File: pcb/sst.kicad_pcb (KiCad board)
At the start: 2 copper layers, 80 x 85 mm, 36 parts, among them X1 CONN_INPUTS, X2 CONN_PWR, X3 CONN_SPI, X4 CONN_I2C, X5 CONN_INPUTS

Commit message: переместил компонент разъёма для ШИМ
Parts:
- moved X5 0.71 mm to (254.8, 145.8)
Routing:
- net GND: track 384.9 -> 382.1 mm
- net Vbat: track 148.7 -> 145.8 mm
- net /<NO NET>: track 50.9 -> 49.3 mm
- net Net-(DD1-PB1): track 19.8 -> 21.3 mm
- net Net-(DD1-PD7): track 27.0 -> 28.2 mm
- net Net-(DD1-PB3): track 30.3 -> 29.4 mm
- net Net-(VD1-A): track 17.9 -> 18.6 mm
- net Net-(DD1-PD5): track 27.2 -> 26.7 mm

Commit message: moved board and set grid origin
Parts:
- moved R6 102.2 mm to (196.5, 137.2)
- moved R8 102.2 mm to (196.5, 105.2)
- moved C1 101.9 mm to (146.9, 100.7)
- moved C2 101.9 mm to (158.3, 112.7)
- moved C3 101.9 mm to (174.8, 98.7)
- moved C4 101.9 mm to (154.3, 151.7)
- moved C5 101.9 mm to (152.0, 141.2)
- moved DA1 101.9 mm to (142.7, 114.6)
- moved HA1 101.9 mm to (139.8, 149.5)
- moved R1 101.9 mm to (180.6, 109.7)
- moved R10 101.9 mm to (131.8, 133.4)
- moved R11 101.9 mm to (133.2, 157.2)
- moved R12 101.9 mm to (143.8, 131.2)
- moved R14 101.9 mm to (137.8, 131.1)
- moved R3 101.9 mm to (179.8, 129.0)
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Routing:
- net Net-(DD1-PC0): track 31.0 -> 29.8 mm
- net Net-(DD1-PB3): track 29.4 -> 30.0 mm

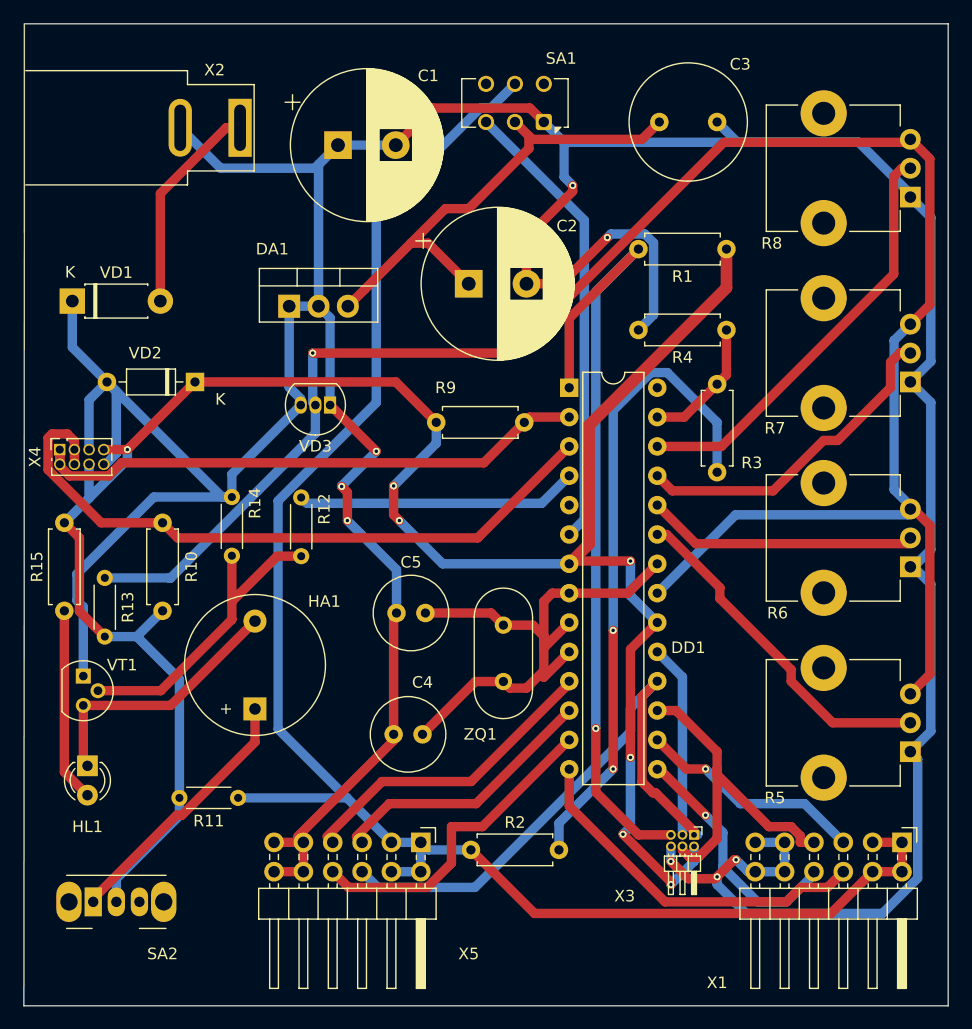
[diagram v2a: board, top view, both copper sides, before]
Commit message: changed geometry, so the demensions would be 80
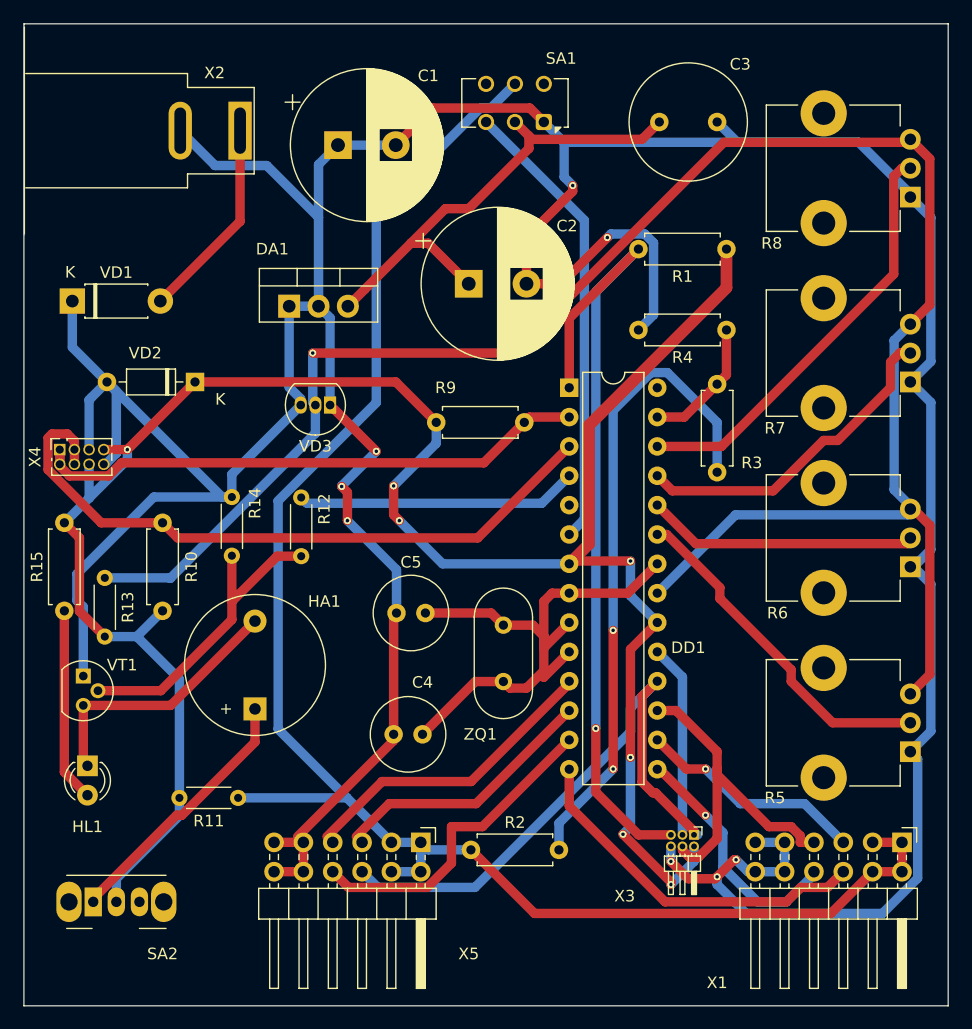
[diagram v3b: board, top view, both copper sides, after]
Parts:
- moved X2 0.25 mm to (138.5, 99.4)
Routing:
- net Net-(VD1-A): track 18.6 -> 17.6 mm
- net GND: track 382.1 -> 381.2 mm
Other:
- outline, holes or cut-outs redrawn
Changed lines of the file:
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@@
 	)
 	(footprint "Connector_BarrelJack:BarrelJack_SwitchcraftConxall_RAPC10U_Horizontal"
-		(locked yes)
 		(layer "F.Cu")
-		(at 138.4656 99.1644)
+		(at 138.4656 99.4144)
 		(descr "DC Power Jack, 13A, 24V, Panel Mount,Through-hole, https://www.switchcraft.com/Drawings/RAPC10U_CD.pdf")
 		(tags "barreljack switchcraftconxall dc power")
@@
 		)
 		(fp_text user "${REFERENCE}"
-			(at -10.4 0 0)
+			(at -10.96 -1 0)
 			(layer "F.Fab")
 			(effects
@@
 	)
 	(gr_line
-		(start 119.7956 90.1644)
+		(start 199.7556 175.1644)
 		(end 199.7556 90.1644)
 		(stroke
@@
 	)
 	(gr_line
-		(start 199.7556 175.1644)
-		(end 199.7556 90.1644)
+		(start 199.7556 90.1644)
+		(end 119.7556 90.1644)
 		(stroke
 			(width 0.05)
@@
 	)
 	(gr_line
-		(start 199.7556 175.1644)
+		(start 119.7556 90.1644)
 		(end 119.7556 175.1644)
 		(stroke
@@
 	)
 	(gr_line
-		(start 119.7956 108.1644)
+		(start 199.7556 175.1644)
 		(end 119.7556 175.1644)
 		(stroke
@@
 	)
 	(segment
-		(start 136.7856 102.6644)
-		(end 133.2856 99.1644)
-		(width 0.8128)
-		(layer "B.Cu")
-		(net 1)
-	)
-	(segment
 		(start 197.1136 164.116903)
 		(end 197.1136 153.7974)
@@
 	)
 	(segment
+		(start 145.2556 106.9144)
+		(end 145.2556 102.349185)
+		(width 0.8128)
+		(layer "B.Cu")
+		(net 1)
+	)
+	(segment
 		(start 198.2556 106.9394)
 		(end 198.2556 119.3894)
@@
 	)
 	(segment
-		(start 145.2556 114.6094)
-		(end 145.2556 102.349185)
+		(start 133.2856 99.4144)
+		(end 136.3036 102.4324)
 		(width 0.8128)
 		(layer "B.Cu")
@@
 	)
 	(segment
+		(start 145.2556 114.6094)
+		(end 145.2556 106.9144)
+		(width 0.8128)
+		(layer "B.Cu")
+		(net 1)
+	)
+	(segment
 		(start 143.7156 123.1844)
 		(end 143.7156 123.1644)
@@
 	)
 	(segment
+		(start 136.3036 102.4324)
+		(end 140.7736 102.4324)
+		(width 0.8128)
+		(layer "B.Cu")
+		(net 1)
+	)
+	(segment
 		(start 125.3956 122.7144)
 		(end 125.3956 127.0194)
@@
 	)
 	(segment
-		(start 146.940385 100.6644)
-		(end 144.940385 102.6644)
+		(start 140.7736 102.4324)
+		(end 145.2556 106.9144)
 		(width 0.8128)
 		(layer "B.Cu")
@@
 	)
 	(segment
-		(start 144.940385 102.6644)
-		(end 136.7856 102.6644)
-		(width 0.8128)
-		(layer "B.Cu")
-		(net 1)
-	)
-	(segment
 		(start 166.5136 100.4224)
 		(end 166.5136 103.4224)
@@
 	)
 	(segment
-		(start 137.2556 99.1644)
-		(end 138.4656 99.1644)
-		(width 0.8128)
-		(layer "F.Cu")
-		(net 34)
-	)
-	(segment
-		(start 131.5656 104.8544)
-		(end 137.2556 99.1644)
+		(start 138.4656 99.4144)
+		(end 138.4656 107.2644)
 		(width 0.8128)
 		(layer "F.Cu")
@@
 	)
 	(segment
-		(start 131.5656 114.1644)
-		(end 131.5656 104.8544)
+		(start 138.4656 107.2644)
+		(end 131.5656 114.1644)
 		(width 0.8128)
 		(layer "F.Cu")
